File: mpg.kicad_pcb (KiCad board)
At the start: 2 copper layers, 90 x 53.3 mm, 83 parts, among them J1 DB25_Male_MountingHoles, J2 Conn_01x04_Male, J3 Conn_01x03_Male, J4 Conn_01x02_Male, J5 RJ45_Shielded, Q1 BC847, Q2 BC847, Q3 BC847, Q4 BC847, Q5 BC847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

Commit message: Final layout.
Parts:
- moved SW1 21.5 mm to (169.9, 66.9), turned to 270 degrees
- moved R2 19.8 mm to (107.2, 70.2), turned to 0 degrees
- moved D2 15.6 mm to (102.9, 70.2), turned to 0 degrees
- moved C8 14.8 mm to (107.2, 66.3), turned to 180 degrees
- moved C6 14.1 mm to (109.0, 77.0), turned to 180 degrees
- moved U1 11.2 mm to (104.8, 60.8), turned to 90 degrees
- moved C10 10.3 mm to (98.1, 77.0), turned to 0 degrees
- moved C5 9.38 mm to (102.6, 66.3), turned to 0 degrees
- moved Q2 7.69 mm to (115.1, 60.8)
- moved Q3 7.69 mm to (120.7, 60.8)
- moved Q4 7.69 mm to (126.2, 60.8)
- moved R4 7.69 mm to (115.1, 64.9)
- moved R5 7.69 mm to (120.7, 64.9)
- moved R7 7.69 mm to (126.2, 64.9)
- moved Q5 7.69 mm to (131.8, 60.8)
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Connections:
- C6 pad 1: Net-(C6-Pad1) -> +12V
- C8 pad 1: Net-(C6-Pad1) -> +12V
- D1 pad 1: +12V -> Net-(D1-Pad1)
- FB1 pad 1: Net-(C6-Pad1) -> +12V
- FB1 pad 2: +12V -> Net-(D1-Pad1)
- R2 pad 2: Net-(C6-Pad1) -> +12V
- U1 pad 3: Net-(C6-Pad1) -> +12V

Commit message: Basic routing.
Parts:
- moved C6 21.1 mm to (92.6, 90.4), turned to 90 degrees
- moved U1 13.0 mm to (98.0, 72.0), turned to 180 degrees
- moved C10 13.0 mm to (111.0, 78.3)
- moved R2 9.67 mm to (109.5, 60.8), turned to 180 degrees
- moved D2 8.49 mm to (109.5, 64.9), turned to 180 degrees
- moved C5 7.76 mm to (104.7, 73.7)
- moved U4 7.60 mm to (100.0, 89.7)
- moved C7 7.13 mm to (159.0, 63.6), turned to 180 degrees
- moved R3 7.13 mm to (159.0, 60.8), turned to 0 degrees
- moved J4 5.12 mm to (106.1, 89.2), turned to 90 degrees
- moved C8 4.68 mm to (104.7, 70.2), turned to 0 degrees
- moved R8 4.34 mm to (103.3, 85.8), turned to 180 degrees
- moved J3 3.61 mm to (144.0, 62.6)
- moved FB1 0.25 mm to (92.7, 97.4)
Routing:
- net +12V: track 0.00 -> 225.9 mm, vias 0 -> 4
- net CAN_H: track 0.00 -> 54.3 mm
- net CAN_L: track 0.00 -> 43.6 mm
- net AXIS_Y: track 0.00 -> 43.3 mm
- net AXIS_B: track 0.00 -> 42.8 mm
- net AXIS_A: track 0.00 -> 42.2 mm
- net AXIS_Z: track 0.00 -> 41.6 mm
- net AXIS_C: track 0.00 -> 38.2 mm
- net X1: track 0.00 -> 32.9 mm
- net X10: track 0.00 -> 31.3 mm
- net POW: track 0.00 -> 26.6 mm
- net +3V3: track 0.00 -> 23.7 mm
- net STOP: track 0.00 -> 19.4 mm
- net AXIS_X: track 0.00 -> 18.2 mm
- net USART1_RX: track 0.00 -> 17.7 mm
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- added copper zone on In2.Cu, net +3V3
- added copper zone on F.Cu, net GND
- added copper zone on In1.Cu, net GND
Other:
- copper layers 2 -> 4

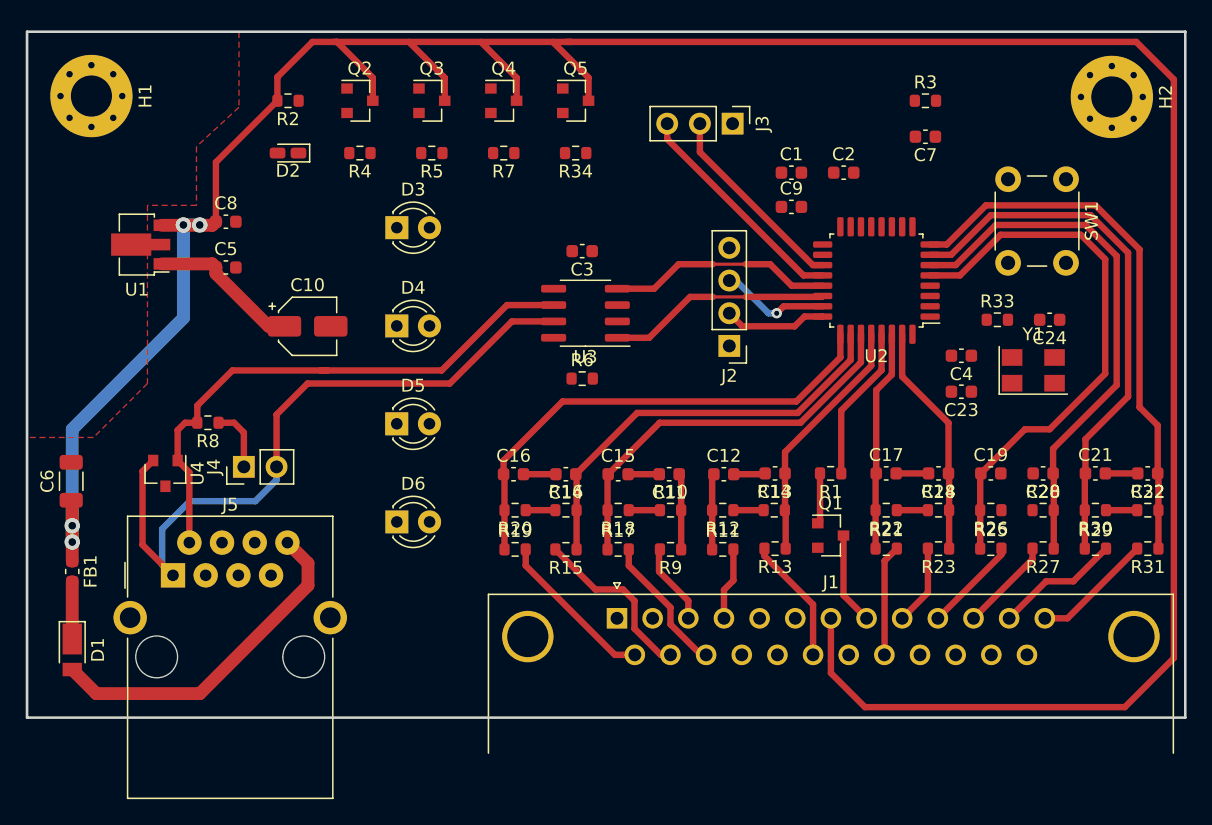
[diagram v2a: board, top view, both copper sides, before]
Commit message: Completed manual track routing.
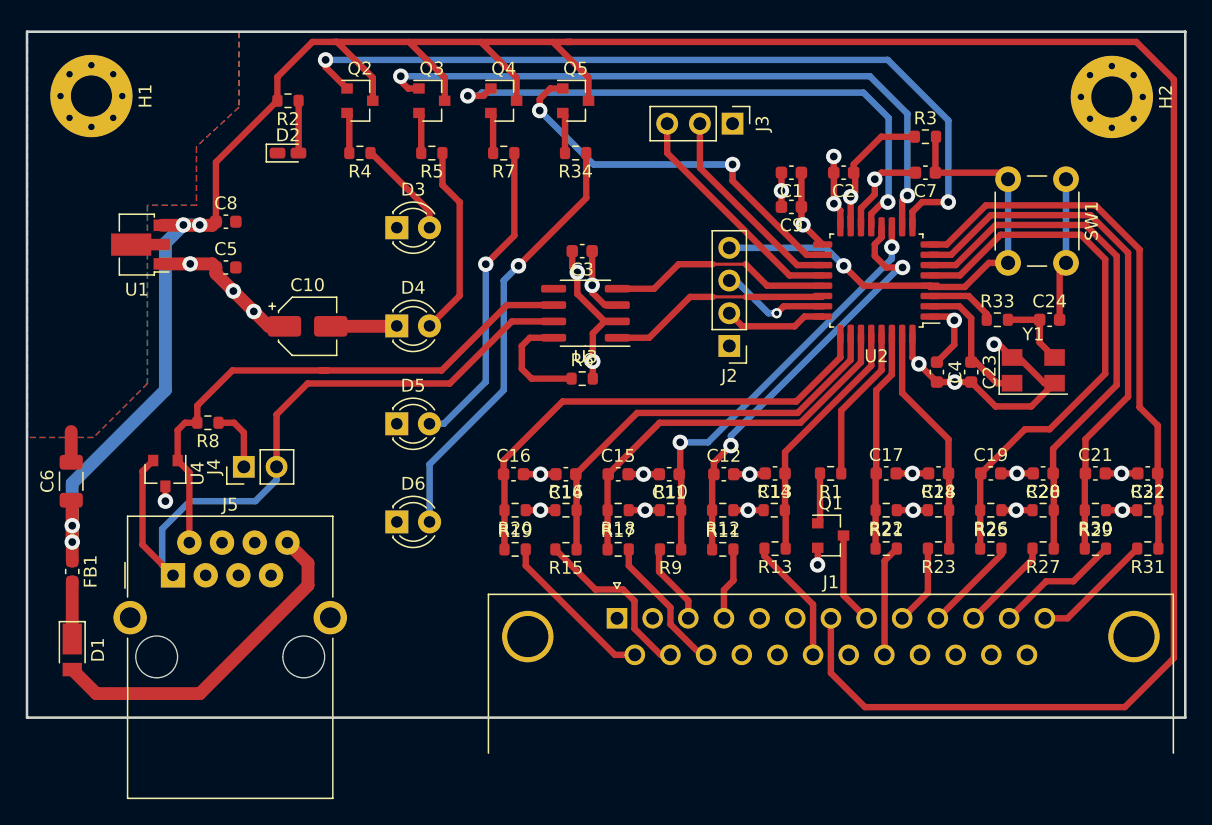
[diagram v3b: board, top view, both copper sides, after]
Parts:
- moved R3 2.79 mm to (159.0, 63.6)
- moved C7 2.79 mm to (159.0, 66.4)
- moved C4 2.29 mm to (159.9, 81.9), turned to 270 degrees
- moved C23 1.70 mm to (162.6, 81.9), turned to 270 degrees
- turned C1 to 180 degrees
- turned C2 to 180 degrees
- turned C24 to 0 degrees
- turned C9 to 180 degrees
- turned D2 to 0 degrees
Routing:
- net GND: track 12.4 -> 85.4 mm, vias 0 -> 17
- net LED_A: track 0.00 -> 63.9 mm, vias 0 -> 2
- net LED_B: track 0.00 -> 51.6 mm, vias 0 -> 2
- net LED_C: track 0.00 -> 44.9 mm, vias 0 -> 2
- net RESET: track 0.00 -> 38.9 mm, vias 0 -> 1
- net Net-(D6-Pad2): track 0.00 -> 33.7 mm, vias 0 -> 1
- net +3V3: track 23.7 -> 54.5 mm, vias 0 -> 13
- net LED_D: track 0.00 -> 30.4 mm, vias 0 -> 2
- net ENC_A: track 5.91 -> 33.2 mm, vias 0 -> 2
- net ENC_B: track 5.90 -> 33.2 mm, vias 0 -> 2
- net Net-(D5-Pad2): track 0.00 -> 24.4 mm, vias 0 -> 1
- net Net-(D4-Pad2): track 0.00 -> 15.0 mm
- net Net-(C23-Pad1): track 0.00 -> 10.8 mm
- net Net-(R6-Pad1): track 0.00 -> 8.71 mm
- net Net-(D3-Pad2): track 0.00 -> 7.73 mm
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- added copper zone on B.Cu, net GND

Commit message: Pours and soldermask.
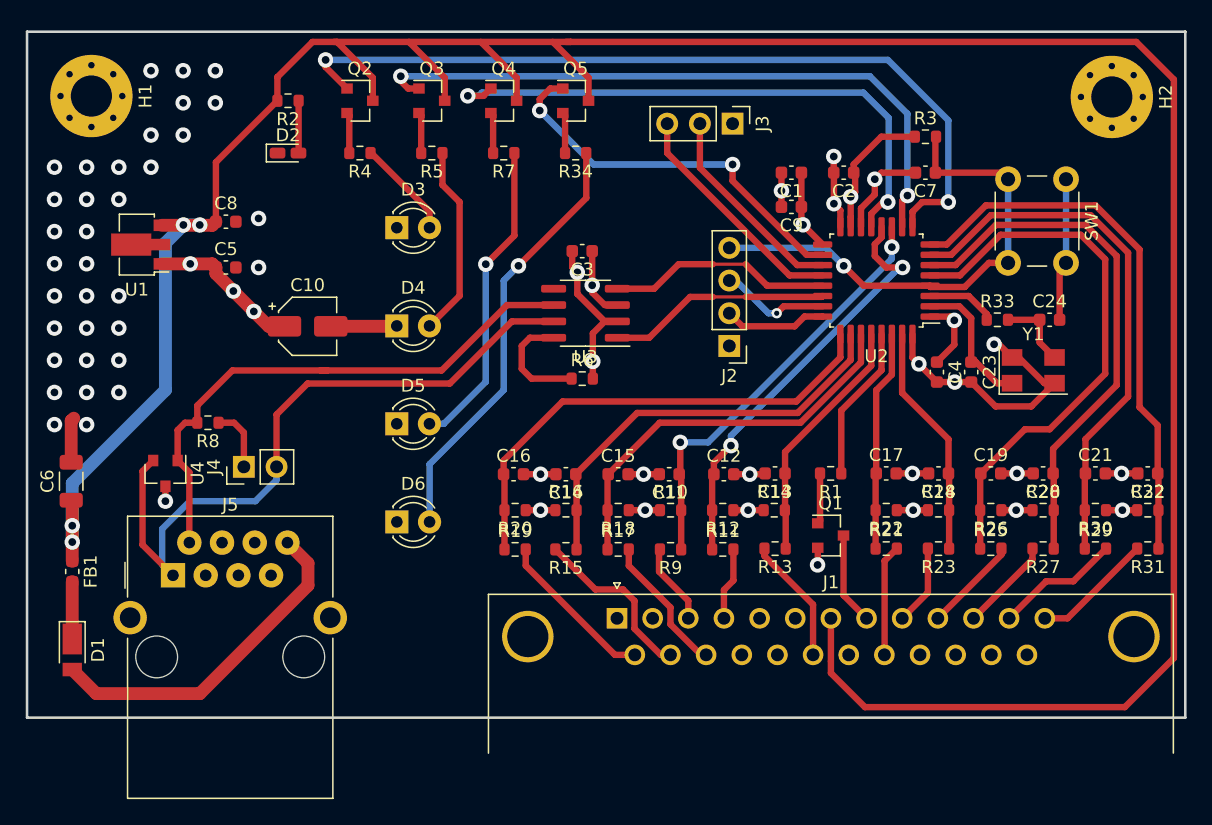
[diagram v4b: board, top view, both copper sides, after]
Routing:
- net GND: track 85.4 -> 86.5 mm, vias 17 -> 51
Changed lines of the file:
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@@
     (thickness 1.6)
     (drawings 140)
-    (tracks 486)
+    (tracks 521)
     (zones 0)
     (modules 83)
@@
   )
   (setup
-    (last_trace_width 0.5)
+    (last_trace_width 1)
     (user_trace_width 0.5)
     (user_trace_width 0.75)
@@
     (trace_clearance 0.2)
     (zone_clearance 0.508)
-    (zone_45_only no)
+    (zone_45_only yes)
     (trace_min 0.2)
     (via_size 0.8)
@@
   (segment (start 117.90864 78.316) (end 117.93912 78.28552) (width 1) (layer F.Cu) (net 65))
   (segment (start 112.81 78.316) (end 117.90864 78.316) (width 1) (layer F.Cu) (net 65))
-  (segment (start 92.64 88.879) (end 92.64 86.489) (width 1) (layer F.Cu) (net 65))
   (segment (start 99.961 90.746) (end 99.961 91.905) (width 0.5) (layer F.Cu) (net 65))
   (via (at 99.961 91.905) (size 1.2) (drill 0.6) (layers F.Cu B.Cu) (net 65))
@@
   (segment (start 154.006 69.145264) (end 155.078986 68.072278) (width 0.5) (layer F.Cu) (net 65))
   (segment (start 154.006 70.585) (end 154.006 69.145264) (width 0.5) (layer F.Cu) (net 65))
+  (via (at 93.84 78.454) (size 1.2) (drill 0.6) (layers F.Cu B.Cu) (net 65))
+  (via (at 93.84 80.954) (size 1.2) (drill 0.6) (layers F.Cu B.Cu) (net 65))
+  (via (at 93.84 83.454) (size 1.2) (drill 0.6) (layers F.Cu B.Cu) (net 65))
+  (via (at 96.34 83.454) (size 1.2) (drill 0.6) (layers F.Cu B.Cu) (net 65))
+  (via (at 96.34 80.954) (size 1.2) (drill 0.6) (layers F.Cu B.Cu) (net 65))
+  (via (at 96.34 78.454) (size 1.2) (drill 0.6) (layers F.Cu B.Cu) (net 65))
+  (via (at 93.84 75.954) (size 1.2) (drill 0.6) (layers F.Cu B.Cu) (net 65))
+  (via (at 93.84 73.454) (size 1.2) (drill 0.6) (layers F.Cu B.Cu) (net 65))
+  (via (at 93.84 70.954) (size 1.2) (drill 0.6) (layers F.Cu B.Cu) (net 65))
+  (via (at 93.84 68.454) (size 1.2) (drill 0.6) (layers F.Cu B.Cu) (net 65))
+  (via (at 93.84 65.954) (size 1.2) (drill 0.6) (layers F.Cu B.Cu) (net 65))
+  (via (at 96.34 65.954) (size 1.2) (drill 0.6) (layers F.Cu B.Cu) (net 65))
+  (via (at 98.84 65.954) (size 1.2) (drill 0.6) (layers F.Cu B.Cu) (net 65))
+  (via (at 96.34 68.454) (size 1.2) (drill 0.6) (layers F.Cu B.Cu) (net 65))
+  (via (at 101.34 63.454) (size 1.2) (drill 0.6) (layers F.Cu B.Cu) (net 65))
+  (via (at 101.34 60.954) (size 1.2) (drill 0.6) (layers F.Cu B.Cu) (net 65))
+  (via (at 101.34 58.454) (size 1.2) (drill 0.6) (layers F.Cu B.Cu) (net 65))
+  (via (at 103.84 58.454) (size 1.2) (drill 0.6) (layers F.Cu B.Cu) (net 65))
+  (via (at 103.84 60.954) (size 1.2) (drill 0.6) (layers F.Cu B.Cu) (net 65))
+  (via (at 96.34 75.954) (size 1.2) (drill 0.6) (layers F.Cu B.Cu) (net 65))
+  (via (at 93.84 85.954) (size 1.2) (drill 0.6) (layers F.Cu B.Cu) (net 65))
+  (via (at 91.34 85.954) (size 1.2) (drill 0.6) (layers F.Cu B.Cu) (net 65))
+  (via (at 91.34 83.454) (size 1.2) (drill 0.6) (layers F.Cu B.Cu) (net 65))
+  (via (at 91.34 80.954) (size 1.2) (drill 0.6) (layers F.Cu B.Cu) (net 65))
+  (via (at 91.34 78.454) (size 1.2) (drill 0.6) (layers F.Cu B.Cu) (net 65))
+  (via (at 91.34 75.954) (size 1.2) (drill 0.6) (layers F.Cu B.Cu) (net 65))
+  (via (at 91.34 73.454) (size 1.2) (drill 0.6) (layers F.Cu B.Cu) (net 65))
+  (via (at 91.34 70.954) (size 1.2) (drill 0.6) (layers F.Cu B.Cu) (net 65))
+  (via (at 91.34 68.454) (size 1.2) (drill 0.6) (layers F.Cu B.Cu) (net 65))
+  (via (at 91.34 65.954) (size 1.2) (drill 0.6) (layers F.Cu B.Cu) (net 65))
+  (segment (start 92.64 85.654) (end 92.84 85.454) (width 1) (layer F.Cu) (net 65))
+  (segment (start 92.64 88.879) (end 92.64 85.654) (width 1) (layer F.Cu) (net 65))
+  (via (at 98.84 63.454) (size 1.2) (drill 0.6) (layers F.Cu B.Cu) (net 65))
+  (via (at 98.84 58.454) (size 1.2) (drill 0.6) (layers F.Cu B.Cu) (net 65))
+  (via (at 107.2 69.934) (size 1.2) (drill 0.6) (layers F.Cu B.Cu) (net 65))
+  (via (at 107.2 73.744) (size 1.2) (drill 0.6) (layers F.Cu B.Cu) (net 65))
   (segment (start 103.607 73.466) (end 103.885 73.744) (width 1) (layer F.Cu) (net 66))
   (segment (start 99.69 73.466) (end 101.89 73.466) (width 1) (layer F.Cu) (net 66))
@@
     (polygon
       (pts
-        (xy 105.676 61.298) (xy 102.374 64.350495) (xy 102.374 68.918) (xy 98.564 68.918) (xy 98.564 82.761)
-        (xy 94.373 86.953) (xy 89.24 86.954) (xy 89.24 55.454) (xy 105.676 55.456)
+        (xy 179.16328 108.7325) (xy 89.23966 108.7325) (xy 89.23966 55.45092) (xy 179.16328 55.45092)
       )
     )
@@
     (polygon
       (pts
-        (xy 105.676 61.298) (xy 102.374 64.350495) (xy 102.374 68.918) (xy 98.564 68.918) (xy 98.564 82.761)
-        (xy 94.373 86.953) (xy 89.24 86.954) (xy 89.24 55.454) (xy 105.676 55.456)
+        (xy 105.676 55.456) (xy 105.676 55.45854) (xy 179.1709 55.45854) (xy 179.1709 108.74266) (xy 89.2295 108.74266)
+        (xy 89.2295 55.45854) (xy 89.24 55.45854) (xy 89.24 55.454)
+      )
+    )
+  )
+  (zone (net 0) (net_name "") (layer F.Mask) (hatch edge 0.508)
+    (connect_pads (clearance 0.508))
+    (min_thickness 0.254)
+    (fill yes (arc_segments 32) (thermal_gap 0.508) (thermal_bridge_width 0.508))
+    (polygon
+      (pts
+        (xy 105.676 61.30054) (xy 98.564 68.92054) (xy 98.564 82.76354) (xy 94.36284 86.9647) (xy 89.23712 86.95454)
+        (xy 89.23966 86.95454) (xy 89.23458 55.45346) (xy 105.66076 55.44838)
+      )
+    )
+  )
+  (zone (net 0) (net_name "") (layer B.Mask) (hatch edge 0.508)
+    (connect_pads (clearance 0.508))
+    (min_thickness 0.254)
+    (fill yes (arc_segments 32) (thermal_gap 0.508) (thermal_bridge_width 0.508))
+    (polygon
+      (pts
+        (xy 105.67346 55.456) (xy 105.67346 61.30054) (xy 98.564 68.918) (xy 98.55892 82.75592) (xy 94.35776 86.95708)
+        (xy 89.23966 86.95454) (xy 89.23966 55.45346)
       )
     )

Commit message: Silk-screens.
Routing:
- net ENC_B: track 33.2 -> 33.8 mm
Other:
- board text added: "---------- 14 C 15 1 16 10 17 COM 18 - 19 STOP 20 GND 21 100 22 - 23 SHLD 24 SHLD 25 SHLD"
- board text added: "DB25 ---------- 1 +3.3V 2 GND 3 ENC-A 4 ENC-B 5 - 6 - 7 +LED 8 -LED 9 X 10 Y 11 Z 12 A 13 B"
- board text added: "GD"
- board text added: "GND"
- board text added: "MPG"
- board text added: "Marangisto 2021"
- board text added: "RJ45 ---------- 1 CAN-H 2 CAN-L 3 GND 4 - 5 - 6 - 7 GND 8 +12V"
- board text added: "RST"
- board text added: "RX"
- board text added: "Rev A"
- board text added: "SWCK"
- board text added: "SWD"
- board text added: "TX"
